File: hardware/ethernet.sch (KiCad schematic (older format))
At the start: 61 parts, among them IC201 MAX5969x, IC202 KSZ8081RNA, IC203 MAX17503, J201 RJ45, J202 AUX POWER, Y201 25MHz

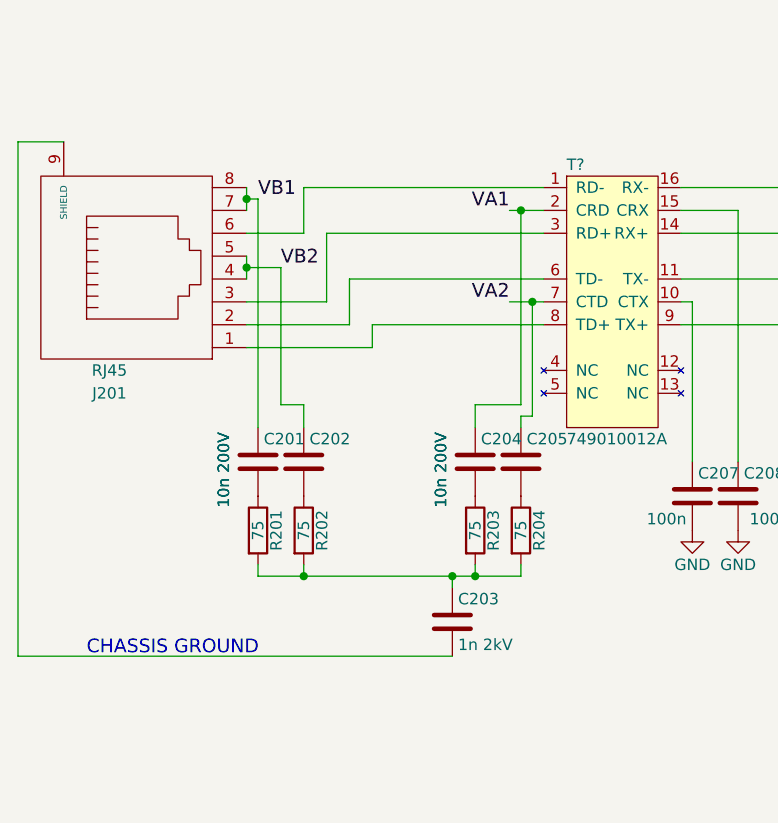
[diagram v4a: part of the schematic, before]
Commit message: Removed pointless half of Bob Smith
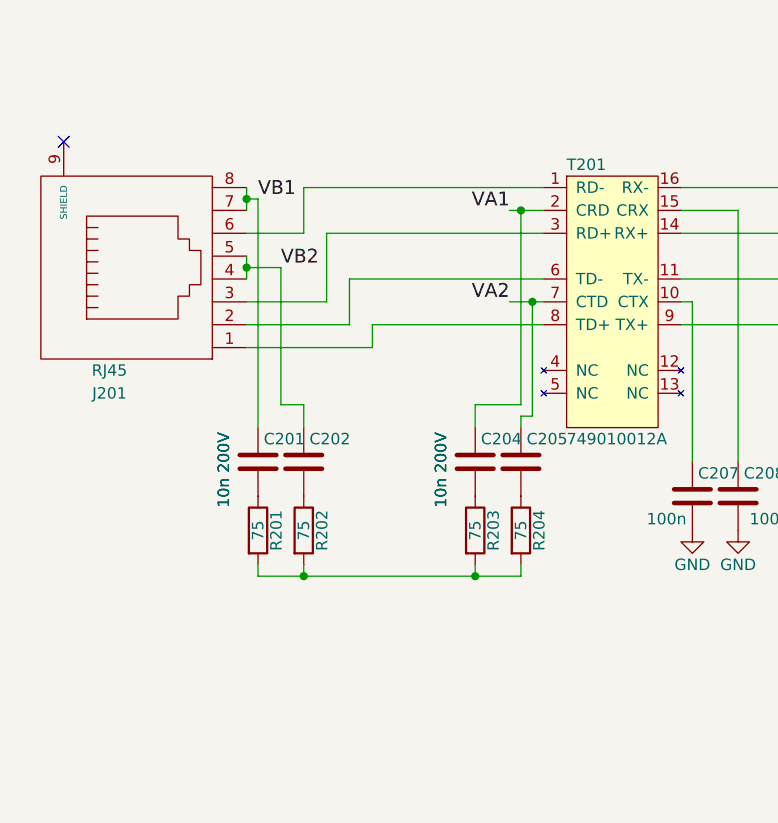
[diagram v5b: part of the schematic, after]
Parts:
- removed C203: 1n 2kV, agg:1206, symbol C
- gave numbers to parts that had none: 1
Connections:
- no-connect marks 7 -> 8
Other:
- note removed: "CHASSIS GROUND"
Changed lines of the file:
@@
 $EndComp
 $Comp
-L +48V #PWR046
+L +48V #PWR8
 U 1 1 57F04B70
 P 5850 4100
-F 0 "#PWR046" H 5850 3950 50  0001 C CNN
+F 0 "#PWR8" H 5850 3950 50  0001 C CNN
 F 1 "+48V" H 5850 4240 50  0000 C CNN
 F 2 "" H 5850 4100 50  0000 C CNN
@@
 $EndComp
 $Comp
-L GND #PWR047
+L GND #PWR9
 U 1 1 57F04B72
 P 5850 4400
-F 0 "#PWR047" H 5850 4150 50  0001 C CNN
+F 0 "#PWR9" H 5850 4150 50  0001 C CNN
 F 1 "GND" H 5850 4250 50  0000 C CNN
 F 2 "" H 5850 4400 50  0000 C CNN
@@
 $EndComp
 $Comp
-L GND #PWR048
+L GND #PWR17
 U 1 1 57F04B74
 P 7900 5600
-F 0 "#PWR048" H 7900 5350 50  0001 C CNN
+F 0 "#PWR17" H 7900 5350 50  0001 C CNN
 F 1 "GND" H 7900 5450 50  0000 C CNN
 F 2 "" H 7900 5600 50  0000 C CNN
@@
 $EndComp
 $Comp
-L GND #PWR049
+L GND #PWR10
 U 1 1 57F04B76
 P 6150 5300
-F 0 "#PWR049" H 6150 5050 50  0001 C CNN
+F 0 "#PWR10" H 6150 5050 50  0001 C CNN
 F 1 "GND" H 6150 5150 50  0000 C CNN
 F 2 "" H 6150 5300 50  0000 C CNN
@@
 $EndComp
 $Comp
-L GND #PWR050
+L GND #PWR14
 U 1 1 57F04B77
 P 6450 5550
-F 0 "#PWR050" H 6450 5300 50  0001 C CNN
+F 0 "#PWR14" H 6450 5300 50  0001 C CNN
 F 1 "GND" H 6450 5400 50  0000 C CNN
 F 2 "" H 6450 5550 50  0000 C CNN
@@
 $EndComp
 $Comp
-L GND #PWR051
+L GND #PWR20
 U 1 1 57F04B7B
 P 8650 5000
-F 0 "#PWR051" H 8650 4750 50  0001 C CNN
+F 0 "#PWR20" H 8650 4750 50  0001 C CNN
 F 1 "GND" H 8650 4850 50  0000 C CNN
 F 2 "" H 8650 5000 50  0000 C CNN
@@
 $EndComp
 $Comp
-L +6V #PWR052
+L +6V #PWR26
 U 1 1 57F04B7C
 P 9900 4550
-F 0 "#PWR052" H 9900 4400 50  0001 C CNN
+F 0 "#PWR26" H 9900 4400 50  0001 C CNN
 F 1 "+6V" H 9900 4690 50  0000 C CNN
 F 2 "" H 9900 4550 50  0000 C CNN
@@
 $EndComp
 $Comp
-L GND #PWR053
+L GND #PWR22
 U 1 1 57F04B7F
 P 9250 5200
-F 0 "#PWR053" H 9250 4950 50  0001 C CNN
+F 0 "#PWR22" H 9250 4950 50  0001 C CNN
 F 1 "GND" H 9250 5050 50  0000 C CNN
 F 2 "" H 9250 5200 50  0000 C CNN
@@
 $EndComp
 $Comp
-L +48V #PWR054
+L +48V #PWR5
 U 1 1 57F04B83
 P 5200 5750
-F 0 "#PWR054" H 5200 5600 50  0001 C CNN
+F 0 "#PWR5" H 5200 5600 50  0001 C CNN
 F 1 "+48V" H 5200 5890 50  0000 C CNN
 F 2 "" H 5200 5750 50  0000 C CNN
@@
 $EndComp
 $Comp
-L GND #PWR055
+L GND #PWR4
 U 1 1 57F04B84
 P 4900 6600
-F 0 "#PWR055" H 4900 6350 50  0001 C CNN
+F 0 "#PWR4" H 4900 6350 50  0001 C CNN
 F 1 "GND" H 4900 6450 50  0000 C CNN
 F 2 "" H 4900 6600 50  0000 C CNN
@@
 $EndComp
 $Comp
-L GND #PWR056
+L GND #PWR1
 U 1 1 57F04B8D
 P 3500 2750
-F 0 "#PWR056" H 3500 2500 50  0001 C CNN
+F 0 "#PWR1" H 3500 2500 50  0001 C CNN
 F 1 "GND" H 3500 2600 50  0000 C CNN
 F 2 "" H 3500 2750 50  0000 C CNN
@@
 $EndComp
 $Comp
-L GND #PWR057
+L GND #PWR2
 U 1 1 57F04B8E
 P 3700 2750
-F 0 "#PWR057" H 3700 2500 50  0001 C CNN
+F 0 "#PWR2" H 3700 2500 50  0001 C CNN
 F 1 "GND" H 3700 2600 50  0000 C CNN
 F 2 "" H 3700 2750 50  0000 C CNN
@@
 $EndComp
 $Comp
-L C C203
-U 1 1 57F04B91
-P 2450 3150
-F 0 "C203" H 2475 3250 50  0000 L CNN
-F 1 "1n 2kV" H 2475 3050 50  0000 L CNN
-F 2 "agg:1206" H 2488 3000 50  0001 C CNN
-F 3 "http://www.farnell.com/datasheets/1958513.pdf" H 2450 3150 50  0001 C CNN
-F 4 "2497062" H 2450 3150 60  0001 C CNN "Farnell"
-	1    2450 3150
-	1    0    0    -1
-$EndComp
-$Comp
 L ZENER D209
 U 1 1 57F04B93
@@
 $EndComp
 $Comp
-L GND #PWR059
+L GND #PWR21
 U 1 1 57F04B97
 P 8850 5000
-F 0 "#PWR059" H 8850 4750 50  0001 C CNN
+F 0 "#PWR21" H 8850 4750 50  0001 C CNN
 F 1 "GND" H 8850 4850 50  0000 C CNN
 F 2 "" H 8850 5000 50  0000 C CNN
@@
 $EndComp
 $Comp
-L GND #PWR060
+L GND #PWR13
 U 1 1 57F04B98
 P 6450 4800
-F 0 "#PWR060" H 6450 4550 50  0001 C CNN
+F 0 "#PWR13" H 6450 4550 50  0001 C CNN
 F 1 "GND" H 6450 4650 50  0000 C CNN
 F 2 "" H 6450 4800 50  0000 C CNN
@@
 TXD1
 $Comp
-L GND #PWR061
+L GND #PWR16
 U 1 1 57F09193
 P 6750 1500
-F 0 "#PWR061" H 6750 1250 50  0001 C CNN
+F 0 "#PWR16" H 6750 1250 50  0001 C CNN
 F 1 "GND" H 6750 1350 50  0000 C CNN
 F 2 "" H 6750 1500 50  0000 C CNN
@@
 $EndComp
 $Comp
-L GND #PWR062
+L GND #PWR11
 U 1 1 57F0CFE9
 P 6250 1500
-F 0 "#PWR062" H 6250 1250 50  0001 C CNN
+F 0 "#PWR11" H 6250 1250 50  0001 C CNN
 F 1 "GND" H 6250 1350 50  0000 C CNN
 F 2 "" H 6250 1500 50  0000 C CNN
@@
 $EndComp
 $Comp
-L GND #PWR063
+L GND #PWR12
 U 1 1 57F0D078
 P 6450 1500
-F 0 "#PWR063" H 6450 1250 50  0001 C CNN
+F 0 "#PWR12" H 6450 1250 50  0001 C CNN
 F 1 "GND" H 6450 1350 50  0000 C CNN
 F 2 "" H 6450 1500 50  0000 C CNN
@@
 $EndComp
 $Comp
-L 3v3 #PWR064
+L 3v3 #PWR6
 U 1 1 57F0D67E
 P 5450 650
-F 0 "#PWR064" H 5450 760 50  0001 L CNN
+F 0 "#PWR6" H 5450 760 50  0001 L CNN
 F 1 "3v3" H 5450 740 50  0000 C CNN
 F 2 "" H 5450 650 60  0001 C CNN
@@
 $EndComp
 $Comp
-L GND #PWR065
+L GND #PWR15
 U 1 1 57F12D2E
 P 6500 2700
-F 0 "#PWR065" H 6500 2450 50  0001 C CNN
+F 0 "#PWR15" H 6500 2450 50  0001 C CNN
 F 1 "GND" H 6500 2550 50  0000 C CNN
 F 2 "" H 6500 2700 50  0000 C CNN
@@
 $EndComp
 $Comp
-L 3v3 #PWR066
+L 3v3 #PWR19
 U 1 1 57F16B5B
 P 8550 1500
-F 0 "#PWR066" H 8550 1610 50  0001 L CNN
+F 0 "#PWR19" H 8550 1610 50  0001 L CNN
 F 1 "3v3" H 8550 1590 50  0000 C CNN
 F 2 "" H 8550 1500 60  0001 C CNN
@@
 $EndComp
 $Comp
-L GND #PWR067
+L GND #PWR18
 U 1 1 57F1933C
 P 8500 2100
-F 0 "#PWR067" H 8500 1850 50  0001 C CNN
+F 0 "#PWR18" H 8500 1850 50  0001 C CNN
 F 1 "GND" H 8500 1950 50  0000 C CNN
 F 2 "" H 8500 2100 50  0000 C CNN
@@
 $EndComp
 $Comp
-L 3v3 #PWR068
+L 3v3 #PWR23
 U 1 1 57F1DF9F
 P 9400 2050
-F 0 "#PWR068" H 9400 2160 50  0001 L CNN
+F 0 "#PWR23" H 9400 2160 50  0001 L CNN
 F 1 "3v3" H 9400 2140 50  0000 C CNN
 F 2 "" H 9400 2050 60  0001 C CNN
@@
 $EndComp
 $Comp
-L GND #PWR069
+L GND #PWR24
 U 1 1 57F1E163
 P 9400 2700
-F 0 "#PWR069" H 9400 2450 50  0001 C CNN
+F 0 "#PWR24" H 9400 2450 50  0001 C CNN
 F 1 "GND" H 9400 2550 50  0000 C CNN
 F 2 "" H 9400 2700 50  0000 C CNN
@@
 GND
 $Comp
-L GND #PWR070
+L GND #PWR25
 U 1 1 57F26BFA
 P 9600 4800
-F 0 "#PWR070" H 9600 4550 50  0001 C CNN
+F 0 "#PWR25" H 9600 4550 50  0001 C CNN
 F 1 "GND" H 9600 4650 50  0000 C CNN
 F 2 "" H 9600 4800 50  0000 C CNN
@@
 $EndComp
 $Comp
-L PWR #FLG071
+L PWR #FLG1
 U 1 1 57F5C8CD
 P 10350 4550
-F 0 "#FLG071" H 10350 4710 50  0001 C CNN
+F 0 "#FLG1" H 10350 4710 50  0001 C CNN
 F 1 "PWR" H 10350 4640 50  0000 C CNN
 F 2 "" H 10350 4550 50  0001 C CNN
@@
 $EndComp
 $Comp
-L GND #PWR072
+L GND #PWR3
 U 1 1 57F877E8
 P 4900 1200
-F 0 "#PWR072" H 4900 950 50  0001 C CNN
+F 0 "#PWR3" H 4900 950 50  0001 C CNN
 F 1 "GND" H 4900 1050 50  0000 C CNN
 F 2 "" H 4900 1200 50  0000 C CNN
@@
 $EndComp
 $Comp
-L GND #PWR073
+L GND #PWR7
 U 1 1 57F878B8
 P 5800 1300
-F 0 "#PWR073" H 5800 1050 50  0001 C CNN
+F 0 "#PWR7" H 5800 1050 50  0001 C CNN
 F 1 "GND" H 5800 1150 50  0000 C CNN
 F 2 "" H 5800 1300 50  0000 C CNN
@@
 	2750 2250 2750 2300
 Wire Wire Line
-	2450 2950 2450 3000
-Wire Wire Line
 	2550 2950 2550 2900
-Connection ~ 2450 2950
 Wire Wire Line
 	2750 2950 2750 2900
@@
 	1550 1550 1550 1650
 Wire Wire Line
-	550  3300 2450 3300
-Wire Wire Line
 	1550 1250 1550 1350
 Wire Wire Line
@@
 Connection ~ 1800 2950
 Wire Wire Line
-	750  1050 550  1050
-Wire Wire Line
-	550  1050 550  3300
-Text Notes 850  3300 0    60   ~ 0
-CHASSIS GROUND
-Wire Wire Line
 	3450 1250 4350 1250
 Wire Wire Line
@@
 	4050 2000 6850 2000
 $Comp
-L 749010012A T?
+L 749010012A T201
 U 1 1 57FD8172
 P 3150 1750
-F 0 "T?" H 2950 2350 50  0000 L CNN
+F 0 "T201" H 2950 2350 50  0000 L CNN
 F 1 "749010012A" H 2950 1150 50  0000 L CNN
 F 2 "agg:749010012A" H 2950 1050 50  0001 L CNN
@@
 	1    0    0    -1
 $EndComp
+NoConn ~ 750  1050
 $EndSCHEMATC

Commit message: Lots of placement/routing
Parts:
- removed TP201: +48V, hardware:Test_point_mini, symbol TESTPAD
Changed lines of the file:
@@
 $EndComp
 $Comp
-L +48V #PWR8
+L +48V #PWR046
 U 1 1 57F04B70
 P 5850 4100
-F 0 "#PWR8" H 5850 3950 50  0001 C CNN
+F 0 "#PWR046" H 5850 3950 50  0001 C CNN
 F 1 "+48V" H 5850 4240 50  0000 C CNN
 F 2 "" H 5850 4100 50  0000 C CNN
@@
 $EndComp
 $Comp
-L GND #PWR9
+L GND #PWR047
 U 1 1 57F04B72
 P 5850 4400
-F 0 "#PWR9" H 5850 4150 50  0001 C CNN
+F 0 "#PWR047" H 5850 4150 50  0001 C CNN
 F 1 "GND" H 5850 4250 50  0000 C CNN
 F 2 "" H 5850 4400 50  0000 C CNN
@@
 $EndComp
 $Comp
-L GND #PWR17
+L GND #PWR048
 U 1 1 57F04B74
 P 7900 5600
-F 0 "#PWR17" H 7900 5350 50  0001 C CNN
+F 0 "#PWR048" H 7900 5350 50  0001 C CNN
 F 1 "GND" H 7900 5450 50  0000 C CNN
 F 2 "" H 7900 5600 50  0000 C CNN
@@
 $EndComp
 $Comp
-L GND #PWR10
+L GND #PWR049
 U 1 1 57F04B76
 P 6150 5300
-F 0 "#PWR10" H 6150 5050 50  0001 C CNN
+F 0 "#PWR049" H 6150 5050 50  0001 C CNN
 F 1 "GND" H 6150 5150 50  0000 C CNN
 F 2 "" H 6150 5300 50  0000 C CNN
@@
 $EndComp
 $Comp
-L GND #PWR14
+L GND #PWR050
 U 1 1 57F04B77
 P 6450 5550
-F 0 "#PWR14" H 6450 5300 50  0001 C CNN
+F 0 "#PWR050" H 6450 5300 50  0001 C CNN
 F 1 "GND" H 6450 5400 50  0000 C CNN
 F 2 "" H 6450 5550 50  0000 C CNN
@@
 $EndComp
 $Comp
-L GND #PWR20
+L GND #PWR051
 U 1 1 57F04B7B
 P 8650 5000
-F 0 "#PWR20" H 8650 4750 50  0001 C CNN
+F 0 "#PWR051" H 8650 4750 50  0001 C CNN
 F 1 "GND" H 8650 4850 50  0000 C CNN
 F 2 "" H 8650 5000 50  0000 C CNN
@@
 $EndComp
 $Comp
-L +6V #PWR26
+L +6V #PWR052
 U 1 1 57F04B7C
 P 9900 4550
-F 0 "#PWR26" H 9900 4400 50  0001 C CNN
+F 0 "#PWR052" H 9900 4400 50  0001 C CNN
 F 1 "+6V" H 9900 4690 50  0000 C CNN
 F 2 "" H 9900 4550 50  0000 C CNN
@@
 $EndComp
 $Comp
-L GND #PWR22
+L GND #PWR053
 U 1 1 57F04B7F
 P 9250 5200
-F 0 "#PWR22" H 9250 4950 50  0001 C CNN
+F 0 "#PWR053" H 9250 4950 50  0001 C CNN
 F 1 "GND" H 9250 5050 50  0000 C CNN
 F 2 "" H 9250 5200 50  0000 C CNN
@@
 $EndComp
 $Comp
-L +48V #PWR5
+L +48V #PWR054
 U 1 1 57F04B83
 P 5200 5750
-F 0 "#PWR5" H 5200 5600 50  0001 C CNN
+F 0 "#PWR054" H 5200 5600 50  0001 C CNN
 F 1 "+48V" H 5200 5890 50  0000 C CNN
 F 2 "" H 5200 5750 50  0000 C CNN
@@
 $EndComp
 $Comp
-L GND #PWR4
+L GND #PWR055
 U 1 1 57F04B84
 P 4900 6600
-F 0 "#PWR4" H 4900 6350 50  0001 C CNN
+F 0 "#PWR055" H 4900 6350 50  0001 C CNN
 F 1 "GND" H 4900 6450 50  0000 C CNN
 F 2 "" H 4900 6600 50  0000 C CNN
@@
 $EndComp
 $Comp
-L GND #PWR1
+L GND #PWR056
 U 1 1 57F04B8D
 P 3500 2750
-F 0 "#PWR1" H 3500 2500 50  0001 C CNN
+F 0 "#PWR056" H 3500 2500 50  0001 C CNN
 F 1 "GND" H 3500 2600 50  0000 C CNN
 F 2 "" H 3500 2750 50  0000 C CNN
@@
 $EndComp
 $Comp
-L GND #PWR2
+L GND #PWR057
 U 1 1 57F04B8E
 P 3700 2750
-F 0 "#PWR2" H 3700 2500 50  0001 C CNN
+F 0 "#PWR057" H 3700 2500 50  0001 C CNN
 F 1 "GND" H 3700 2600 50  0000 C CNN
 F 2 "" H 3700 2750 50  0000 C CNN
@@
 $EndComp
 $Comp
-L GND #PWR21
+L GND #PWR058
 U 1 1 57F04B97
 P 8850 5000
-F 0 "#PWR21" H 8850 4750 50  0001 C CNN
+F 0 "#PWR058" H 8850 4750 50  0001 C CNN
 F 1 "GND" H 8850 4850 50  0000 C CNN
 F 2 "" H 8850 5000 50  0000 C CNN
@@
 $EndComp
 $Comp
-L GND #PWR13
+L GND #PWR059
 U 1 1 57F04B98
 P 6450 4800
-F 0 "#PWR13" H 6450 4550 50  0001 C CNN
+F 0 "#PWR059" H 6450 4550 50  0001 C CNN
 F 1 "GND" H 6450 4650 50  0000 C CNN
 F 2 "" H 6450 4800 50  0000 C CNN
@@
 TXD1
 $Comp
-L GND #PWR16
+L GND #PWR060
 U 1 1 57F09193
 P 6750 1500
-F 0 "#PWR16" H 6750 1250 50  0001 C CNN
+F 0 "#PWR060" H 6750 1250 50  0001 C CNN
 F 1 "GND" H 6750 1350 50  0000 C CNN
 F 2 "" H 6750 1500 50  0000 C CNN
@@
 $EndComp
 $Comp
-L GND #PWR11
+L GND #PWR061
 U 1 1 57F0CFE9
 P 6250 1500
-F 0 "#PWR11" H 6250 1250 50  0001 C CNN
+F 0 "#PWR061" H 6250 1250 50  0001 C CNN
 F 1 "GND" H 6250 1350 50  0000 C CNN
 F 2 "" H 6250 1500 50  0000 C CNN
@@
 $EndComp
 $Comp
-L GND #PWR12
+L GND #PWR062
 U 1 1 57F0D078
 P 6450 1500
-F 0 "#PWR12" H 6450 1250 50  0001 C CNN
+F 0 "#PWR062" H 6450 1250 50  0001 C CNN
 F 1 "GND" H 6450 1350 50  0000 C CNN
 F 2 "" H 6450 1500 50  0000 C CNN
@@
 $EndComp
 $Comp
-L 3v3 #PWR6
+L 3v3 #PWR063
 U 1 1 57F0D67E
 P 5450 650
-F 0 "#PWR6" H 5450 760 50  0001 L CNN
+F 0 "#PWR063" H 5450 760 50  0001 L CNN
 F 1 "3v3" H 5450 740 50  0000 C CNN
 F 2 "" H 5450 650 60  0001 C CNN
@@
 $EndComp
 $Comp
-L GND #PWR15
+L GND #PWR064
 U 1 1 57F12D2E
 P 6500 2700
-F 0 "#PWR15" H 6500 2450 50  0001 C CNN
+F 0 "#PWR064" H 6500 2450 50  0001 C CNN
 F 1 "GND" H 6500 2550 50  0000 C CNN
 F 2 "" H 6500 2700 50  0000 C CNN
@@
 $EndComp
 $Comp
-L 3v3 #PWR19
+L 3v3 #PWR065
 U 1 1 57F16B5B
 P 8550 1500
-F 0 "#PWR19" H 8550 1610 50  0001 L CNN
+F 0 "#PWR065" H 8550 1610 50  0001 L CNN
 F 1 "3v3" H 8550 1590 50  0000 C CNN
 F 2 "" H 8550 1500 60  0001 C CNN
@@
 $EndComp
 $Comp
-L GND #PWR18
+L GND #PWR066
 U 1 1 57F1933C
 P 8500 2100
-F 0 "#PWR18" H 8500 1850 50  0001 C CNN
+F 0 "#PWR066" H 8500 1850 50  0001 C CNN
 F 1 "GND" H 8500 1950 50  0000 C CNN
 F 2 "" H 8500 2100 50  0000 C CNN
@@
 $EndComp
 $Comp
-L 3v3 #PWR23
+L 3v3 #PWR067
 U 1 1 57F1DF9F
 P 9400 2050
-F 0 "#PWR23" H 9400 2160 50  0001 L CNN
+F 0 "#PWR067" H 9400 2160 50  0001 L CNN
 F 1 "3v3" H 9400 2140 50  0000 C CNN
 F 2 "" H 9400 2050 60  0001 C CNN
@@
 $EndComp
 $Comp
-L GND #PWR24
+L GND #PWR068
 U 1 1 57F1E163
 P 9400 2700
-F 0 "#PWR24" H 9400 2450 50  0001 C CNN
+F 0 "#PWR068" H 9400 2450 50  0001 C CNN
 F 1 "GND" H 9400 2550 50  0000 C CNN
 F 2 "" H 9400 2700 50  0000 C CNN
@@
 GND
 $Comp
-L GND #PWR25
+L GND #PWR069
 U 1 1 57F26BFA
 P 9600 4800
-F 0 "#PWR25" H 9600 4550 50  0001 C CNN
+F 0 "#PWR069" H 9600 4550 50  0001 C CNN
 F 1 "GND" H 9600 4650 50  0000 C CNN
 F 2 "" H 9600 4800 50  0000 C CNN
@@
 $EndComp
 $Comp
-L TESTPAD TP201
-U 1 1 57F301FA
-P 4900 5700
-F 0 "TP201" H 4900 5750 50  0000 L CNN
-F 1 "+48V" H 4900 5625 50  0000 L CNN
-F 2 "hardware:Test_point_mini" H 4900 5550 50  0001 L CNN
-F 3 "" H 4900 5700 50  0001 C CNN
-	1    4900 5700
-	0    -1   -1   0
-$EndComp
-$Comp
 L TESTPAD TP205
 U 1 1 57F30FDA
@@
 $EndComp
 $Comp
-L PWR #FLG1
+L PWR #FLG070
 U 1 1 57F5C8CD
 P 10350 4550
-F 0 "#FLG1" H 10350 4710 50  0001 C CNN
+F 0 "#FLG070" H 10350 4710 50  0001 C CNN
 F 1 "PWR" H 10350 4640 50  0000 C CNN
 F 2 "" H 10350 4550 50  0001 C CNN
@@
 $EndComp
 $Comp
-L GND #PWR3
+L GND #PWR071
 U 1 1 57F877E8
 P 4900 1200
-F 0 "#PWR3" H 4900 950 50  0001 C CNN
+F 0 "#PWR071" H 4900 950 50  0001 C CNN
 F 1 "GND" H 4900 1050 50  0000 C CNN
 F 2 "" H 4900 1200 50  0000 C CNN
@@
 $EndComp
 $Comp
-L GND #PWR7
+L GND #PWR072
 U 1 1 57F878B8
 P 5800 1300
-F 0 "#PWR7" H 5800 1050 50  0001 C CNN
+F 0 "#PWR072" H 5800 1050 50  0001 C CNN
 F 1 "GND" H 5800 1150 50  0000 C CNN
 F 2 "" H 5800 1300 50  0000 C CNN
@@
 	4800 5750 5200 5750
 Wire Wire Line
-	4900 5750 4900 5700
-Connection ~ 4900 5750
-Wire Wire Line
 	9900 4550 9900 4600

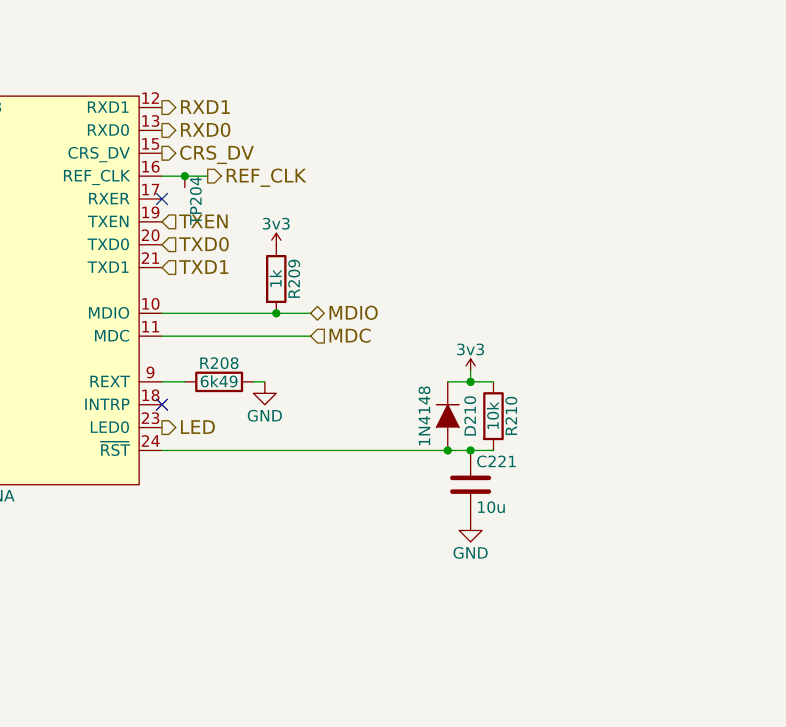
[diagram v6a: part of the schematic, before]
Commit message: Placed uc, routed RMII
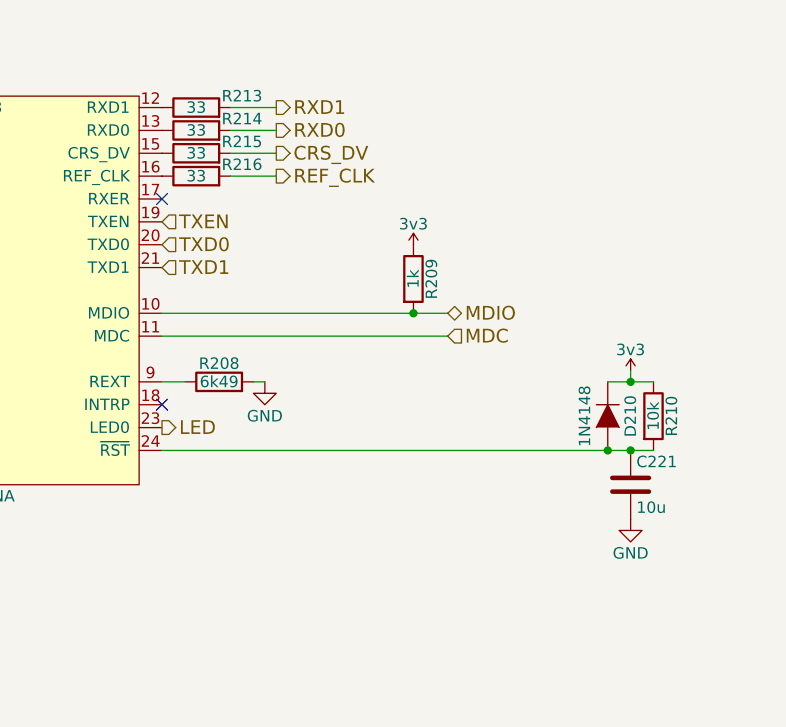
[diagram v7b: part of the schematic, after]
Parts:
- removed TP204: 50MHz_CLK, agg:TESTPAD, symbol TESTPAD
- added R213, R214, R215, R216: 33, agg:0603, symbol R
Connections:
- net CRS_DV: now also R215.2; no longer IC202.15 (CRS_DV)
- net REF_CLK: now also R216.2; no longer IC202.16 (REF_CLK)
- net RXD0: now also R214.2; no longer IC202.13 (RXD0)
- net RXD1: now also R213.2; no longer IC202.12 (RXD1)
- new net: IC202.12 (RXD1), R213.1
- new net: IC202.13 (RXD0), R214.1
- new net: IC202.15 (CRS_DV), R215.1
- new net: IC202.16 (REF_CLK), R216.1
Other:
- moved on the sheet: C221, D210, R209, R210
